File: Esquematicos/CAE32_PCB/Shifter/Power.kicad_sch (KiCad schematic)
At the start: 20 parts, among them J6 USB_C_Receptacle_USB2.0, U3 AP2112K-3.3, U4 USBLC6-2P6

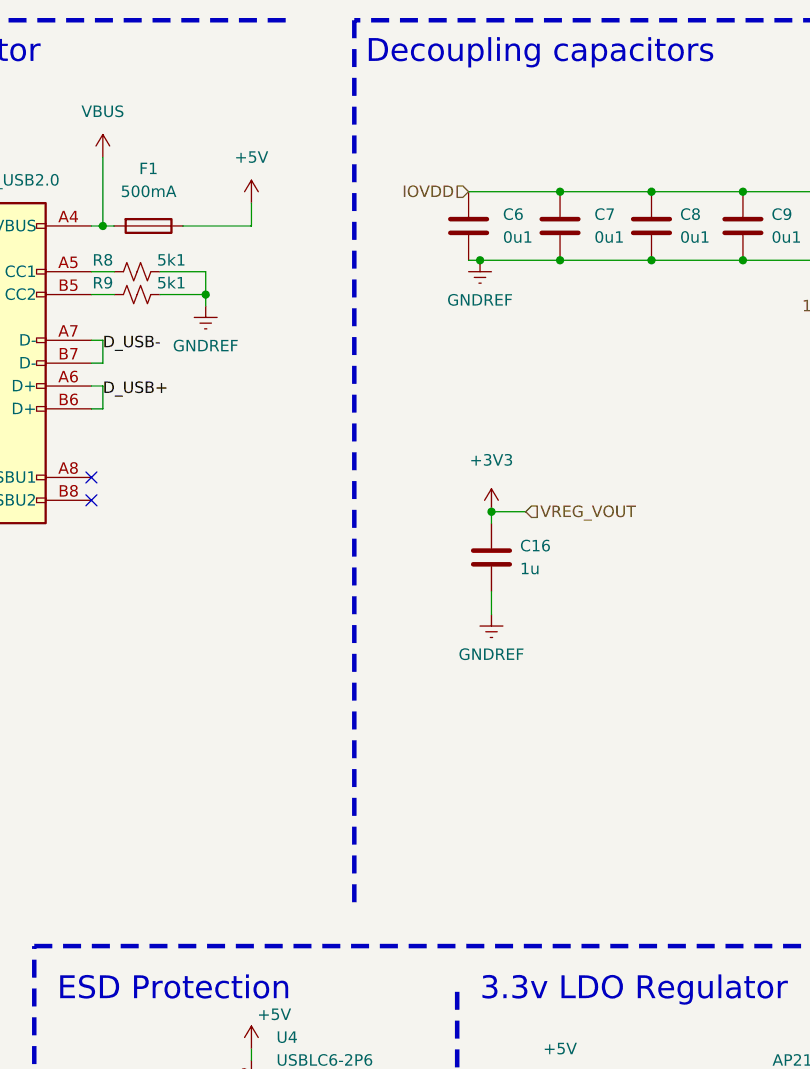
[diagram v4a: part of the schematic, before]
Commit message: update: added minor improvements to Shifter's PCB
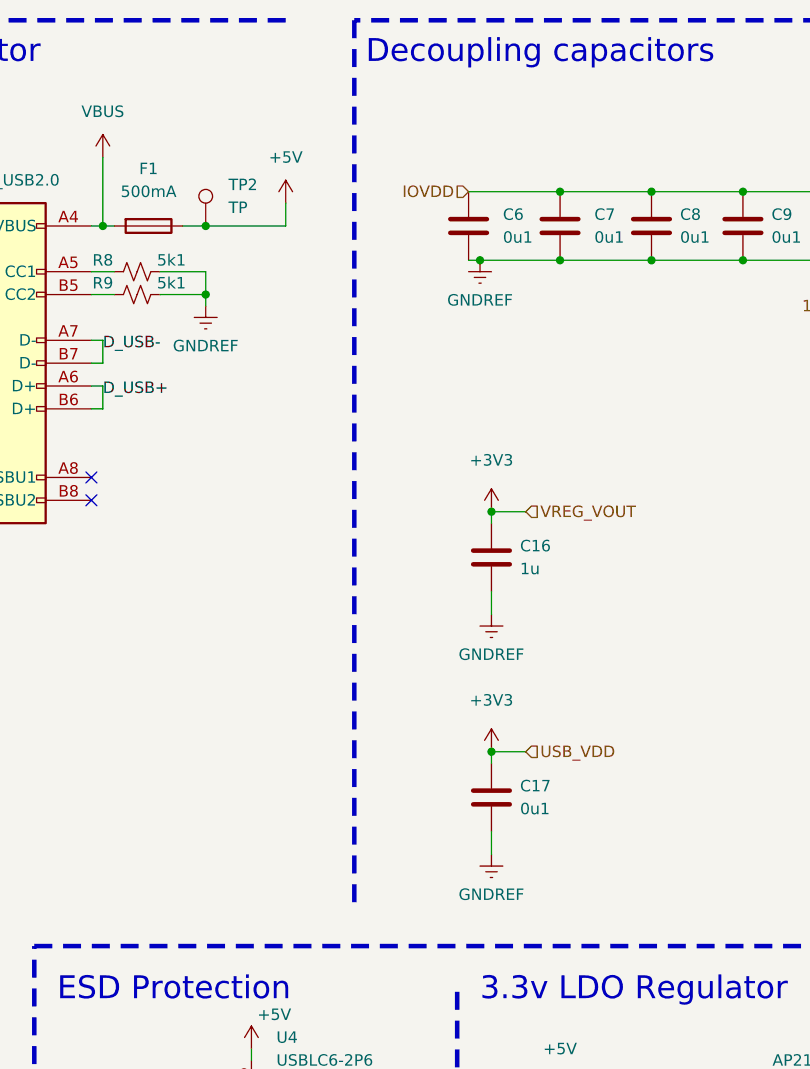
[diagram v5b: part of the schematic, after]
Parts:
- added C17: 0u1, Capacitor_SMD:C_01005_0402Metric, symbol Device:C
- added TP2: TP, TestPoint:TestPoint_Pad_D1.0mm, symbol Connector:TestPoint
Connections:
- net +3V3: now also C17.1
- net +5V: now also TP2.1
- net GNDREF: now also C17.2
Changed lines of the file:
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@@
   (junction (at 240.03 142.24) (diameter 0) (color 0 0 0 0)
   )
+  (junction (at 219.71 102.87) (diameter 0) (color 0 0 0 0)
+  )
   (junction (at 259.08 40.64) (diameter 0) (color 0 0 0 0)
   )
@@
   )
   (junction (at 227.33 48.26) (diameter 0) (color 0 0 0 0)
+  )
+  (junction (at 187.96 44.45) (diameter 0) (color 0 0 0 0)
   )
   (no_connect (at 175.26 72.39))
@@
     (stroke (width 0) (type default))
   )
+  (wire (pts (xy 187.96 44.45) (xy 196.85 44.45))
+    (stroke (width 0) (type default))
+  )
   (wire (pts (xy 227.33 140.97) (xy 227.33 142.24))
     (stroke (width 0) (type default))
@@
   )
   (wire (pts (xy 176.53 44.45) (xy 177.8 44.45))
+    (stroke (width 0) (type default))
+  )
+  (wire (pts (xy 223.52 102.87) (xy 219.71 102.87))
     (stroke (width 0) (type default))
   )
@@
     (stroke (width 0) (type default))
   )
-  (wire (pts (xy 185.42 44.45) (xy 193.04 44.45))
+  (wire (pts (xy 185.42 44.45) (xy 187.96 44.45))
     (stroke (width 0) (type default))
   )
@@
     (stroke (width 0.5) (type dash_dot))
   )
+  (wire (pts (xy 219.71 111.76) (xy 219.71 114.3))
+    (stroke (width 0) (type default))
+  )
   (wire (pts (xy 259.08 53.34) (xy 259.08 55.88))
     (stroke (width 0) (type default))
@@
     (stroke (width 0) (type default))
   )
+  (wire (pts (xy 219.71 102.87) (xy 219.71 104.14))
+    (stroke (width 0) (type default))
+  )
   (wire (pts (xy 176.53 64.77) (xy 175.26 64.77))
     (stroke (width 0) (type default))
@@
     (stroke (width 0) (type default))
   )
-  (wire (pts (xy 193.04 44.45) (xy 193.04 41.91))
+  (wire (pts (xy 196.85 44.45) (xy 196.85 41.91))
     (stroke (width 0) (type default))
   )
@@
     (effects (font (size 1.27 1.27)) (justify left bottom))
   )
+  (hierarchical_label "USB_VDD" (shape input) (at 223.52 102.87 0) (fields_autoplaced)
+    (effects (font (size 1.27 1.27)) (justify left))
+  )
   (hierarchical_label "VREG_IN" (shape input) (at 273.05 104.14 0) (fields_autoplaced)
     (effects (font (size 1.27 1.27)) (justify left))
@@
         (path "/1377ea75-295d-49bc-b9a9-d51d30c69cc4/7750e748-ac9c-453c-8bb6-154f2ada0dc5"
           (reference "#PWR023") (unit 1)
+        )
+      )
+    )
+  )
+  (symbol (lib_id "power:GNDREF") (at 219.71 114.3 0) (unit 1)
+    (in_bom yes) (on_board yes) (dnp no) (fields_autoplaced)
+    (property "Reference" "#PWR044" (at 219.71 120.65 0)
+      (effects (font (size 1.27 1.27)) hide)
+    )
+    (property "Value" "GNDREF" (at 219.71 118.745 0)
+      (effects (font (size 1.27 1.27)))
+    )
+    (property "Footprint" "" (at 219.71 114.3 0)
+      (effects (font (size 1.27 1.27)) hide)
+    )
+    (property "Datasheet" "" (at 219.71 114.3 0)
+      (effects (font (size 1.27 1.27)) hide)
+    )
+    (pin "1")
+    (instances
+      (project "Shifter"
+        (path "/1377ea75-295d-49bc-b9a9-d51d30c69cc4/7750e748-ac9c-453c-8bb6-154f2ada0dc5"
+          (reference "#PWR044") (unit 1)
         )
       )
@@
         (path "/1377ea75-295d-49bc-b9a9-d51d30c69cc4/7750e748-ac9c-453c-8bb6-154f2ada0dc5"
           (reference "C6") (unit 1)
+        )
+      )
+    )
+  )
+  (symbol (lib_id "power:+3V3") (at 219.71 102.87 0) (unit 1)
+    (in_bom yes) (on_board yes) (dnp no) (fields_autoplaced)
+    (property "Reference" "#PWR043" (at 219.71 106.68 0)
+      (effects (font (size 1.27 1.27)) hide)
+    )
+    (property "Value" "+3V3" (at 219.71 97.155 0)
+      (effects (font (size 1.27 1.27)))
+    )
+    (property "Footprint" "" (at 219.71 102.87 0)
+      (effects (font (size 1.27 1.27)) hide)
+    )
+    (property "Datasheet" "" (at 219.71 102.87 0)
+      (effects (font (size 1.27 1.27)) hide)
+    )
+    (pin "1")
+    (instances
+      (project "Shifter"
+        (path "/1377ea75-295d-49bc-b9a9-d51d30c69cc4/7750e748-ac9c-453c-8bb6-154f2ada0dc5"
+          (reference "#PWR043") (unit 1)
+        )
+      )
+    )
+  )
+  (symbol (lib_id "Connector:TestPoint") (at 187.96 44.45 0) (unit 1)
+    (in_bom yes) (on_board yes) (dnp no) (fields_autoplaced)
+    (property "Reference" "TP2" (at 190.5 39.878 0)
+      (effects (font (size 1.27 1.27)) (justify left))
+    )
+    (property "Value" "TP" (at 190.5 42.418 0)
+      (effects (font (size 1.27 1.27)) (justify left))
+    )
+    (property "Footprint" "TestPoint:TestPoint_Pad_D1.0mm" (at 193.04 44.45 0)
+      (effects (font (size 1.27 1.27)) hide)
+    )
+    (property "Datasheet" "~" (at 193.04 44.45 0)
+      (effects (font (size 1.27 1.27)) hide)
+    )
+    (pin "1")
+    (instances
+      (project "Shifter"
+        (path "/1377ea75-295d-49bc-b9a9-d51d30c69cc4/7750e748-ac9c-453c-8bb6-154f2ada0dc5"
+          (reference "TP2") (unit 1)
         )
       )
@@
     )
   )
+  (symbol (lib_id "Device:C") (at 219.71 107.95 0) (unit 1)
+    (in_bom yes) (on_board yes) (dnp no) (fields_autoplaced)
+    (property "Reference" "C17" (at 222.885 106.6799 0)
+      (effects (font (size 1.27 1.27)) (justify left))
+    )
+    (property "Value" "0u1" (at 222.885 109.2199 0)
+      (effects (font (size 1.27 1.27)) (justify left))
+    )
+    (property "Footprint" "Capacitor_SMD:C_01005_0402Metric" (at 220.6752 111.76 0)
+      (effects (font (size 1.27 1.27)) hide)
+    )
+    (property "Datasheet" "~" (at 219.71 107.95 0)
+      (effects (font (size 1.27 1.27)) hide)
+    )
+    (property "Vendor" "C913620" (at 219.71 107.95 0)
+      (effects (font (size 1.27 1.27)) hide)
+    )
+    (pin "1")
+    (pin "2")
+    (instances
+      (project "Shifter"
+        (path "/1377ea75-295d-49bc-b9a9-d51d30c69cc4/7750e748-ac9c-453c-8bb6-154f2ada0dc5"
+          (reference "C17") (unit 1)
+        )
+      )
+    )
+  )
   (symbol (lib_id "Device:R_Small_US") (at 243.84 144.78 270) (unit 1)
     (in_bom yes) (on_board yes) (dnp no)
@@
     )
   )
-  (symbol (lib_id "power:+5V") (at 193.04 41.91 0) (unit 1)
-    (in_bom yes) (on_board yes) (dnp no) (fields_autoplaced)
-    (property "Reference" "#PWR022" (at 193.04 45.72 0)
-      (effects (font (size 1.27 1.27)) hide)
-    )
-    (property "Value" "+5V" (at 193.04 36.83 0)
-      (effects (font (size 1.27 1.27)))
-    )
-    (property "Footprint" "" (at 193.04 41.91 0)
-      (effects (font (size 1.27 1.27)) hide)
-    )
-    (property "Datasheet" "" (at 193.04 41.91 0)
-      (effects (font (size 1.27 1.27)) hide)
-    )
+  (symbol (lib_id "power:+5V") (at 196.85 41.91 0) (unit 1)
+    (in_bom yes) (on_board yes) (dnp no) (fields_autoplaced)
+    (property "Reference" "#PWR022" (at 196.85 45.72 0)
+      (effects (font (size 1.27 1.27)) hide)
+    )
+    (property "Value" "+5V" (at 196.85 36.83 0)
+      (effects (font (size 1.27 1.27)))
+    )
+    (property "Footprint" "" (at 196.85 41.91 0)
+      (effects (font (size 1.27 1.27)) hide)
+    )
+    (property "Datasheet" "" (at 196.85 41.91 0)
+      (effects (font (size 1.27 1.27)) hide)
+    )
